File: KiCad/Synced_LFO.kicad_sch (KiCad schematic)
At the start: 41 parts, among them J1 UP_Out, J2 CLK In, J3 BP_Inv_Out, J4 BP_Out, P1 B100K, P2 B100K, P3 B100K, P4 B100K, U1 TL072, U2 TL072

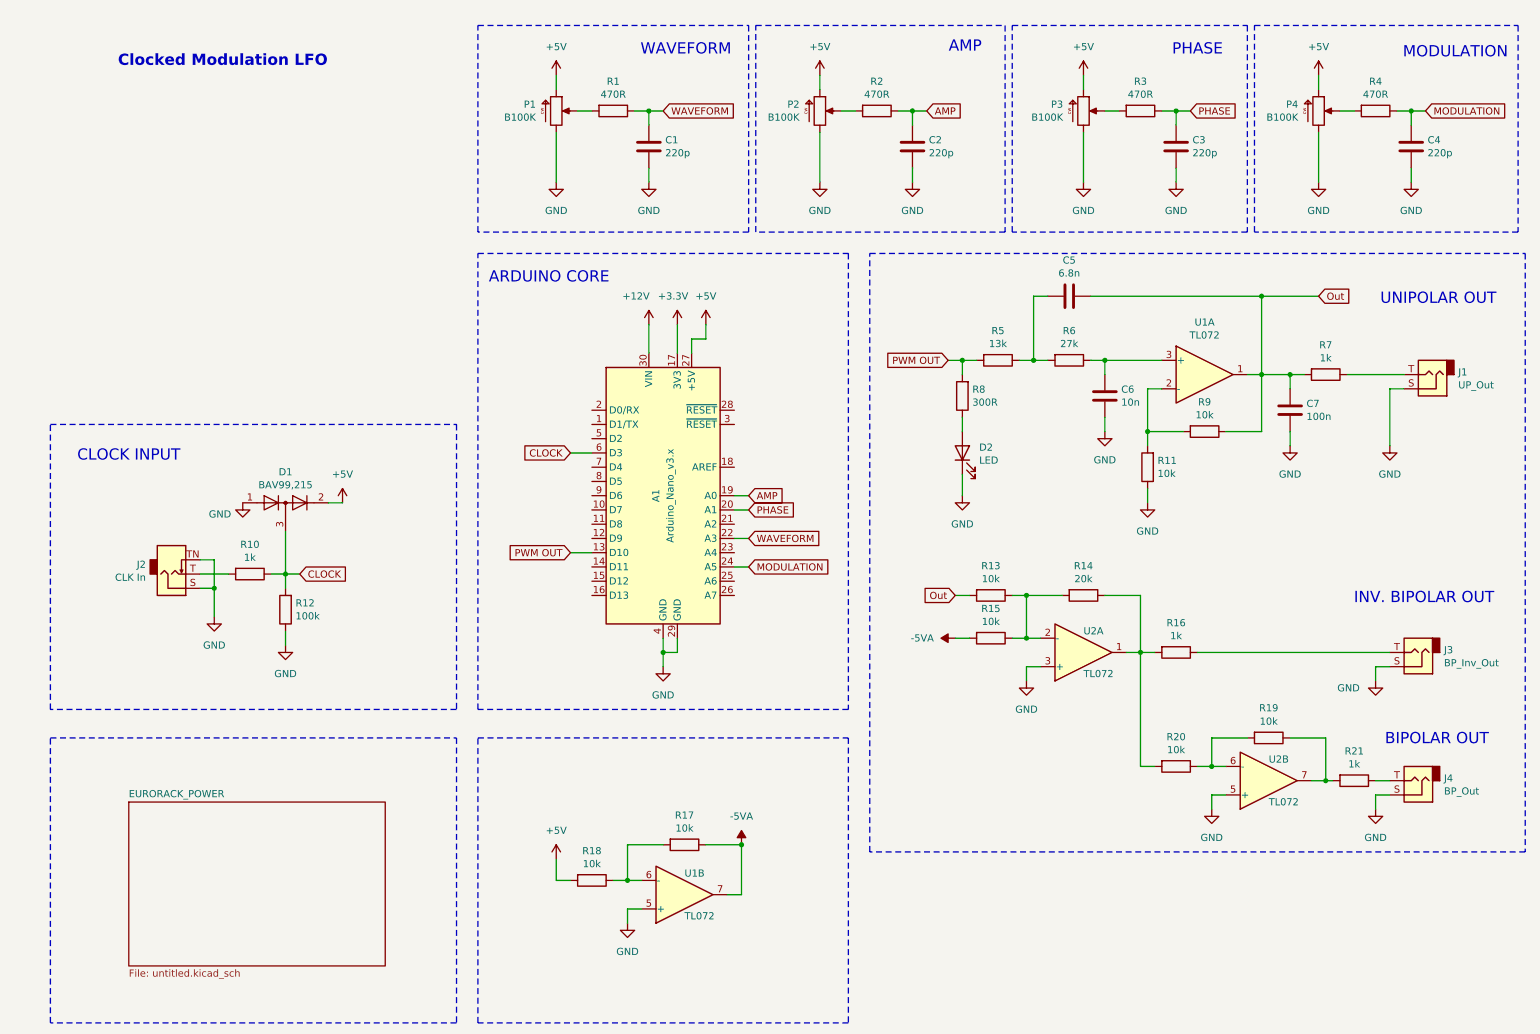
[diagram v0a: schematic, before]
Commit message: Added new Powerrail and fixed ERC Error
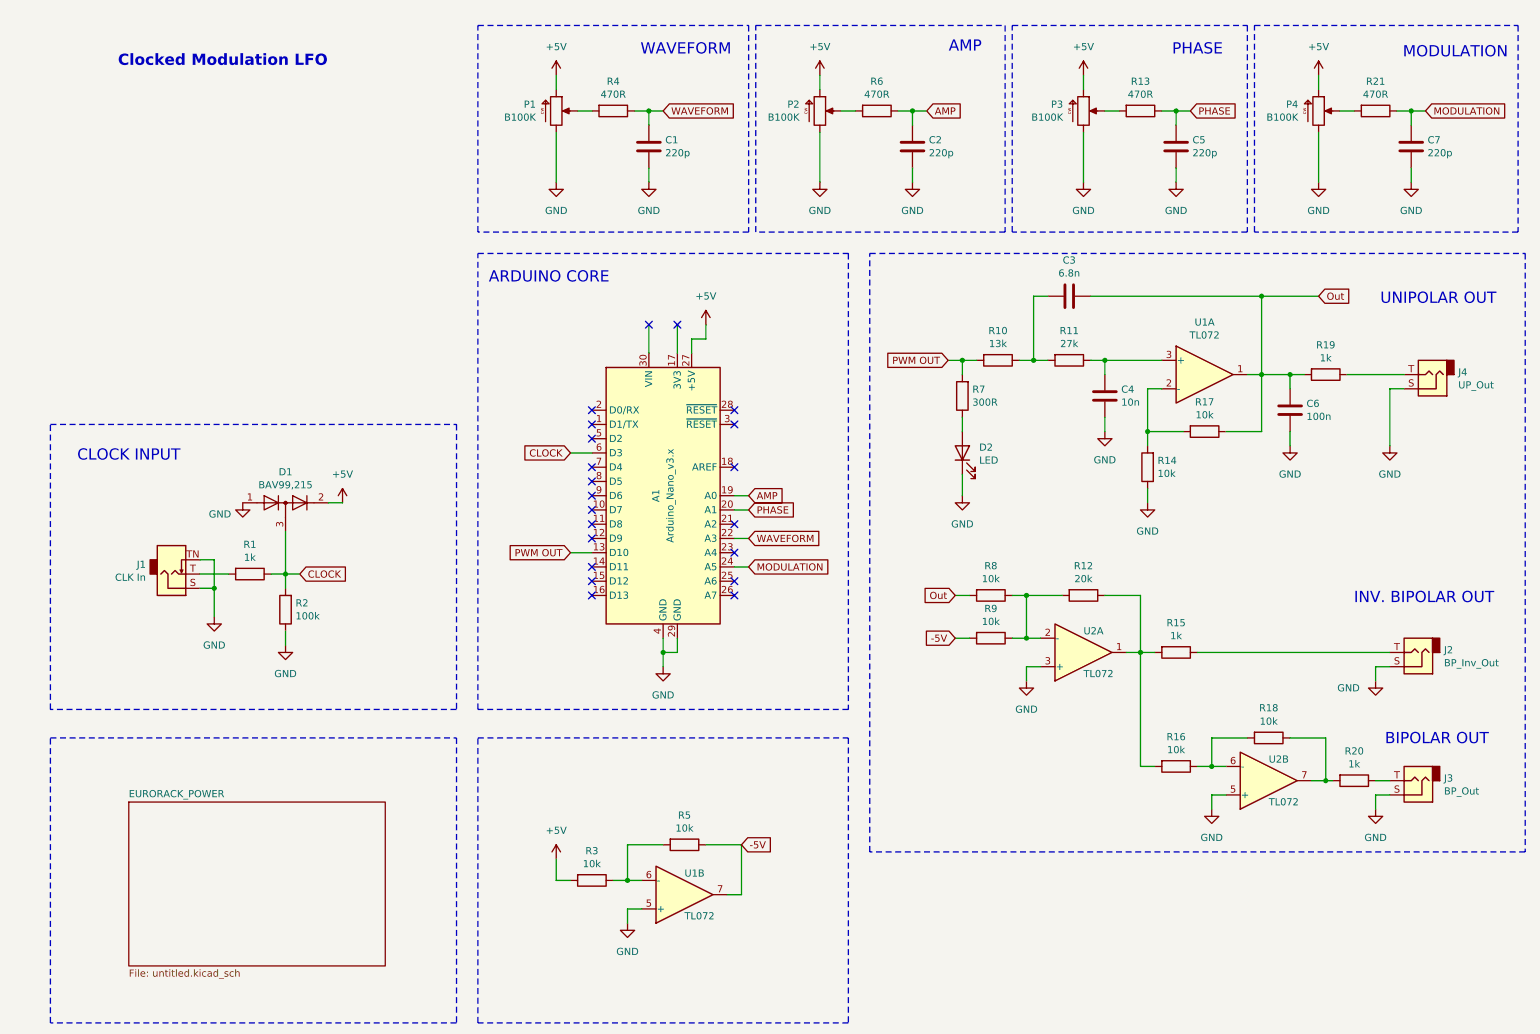
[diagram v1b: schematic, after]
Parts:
- renumbered C5 to C3, C6 to C4, C3 to C5, C7 to C6, C4 to C7, J2 to J1, J3 to J2, J4 to J3, J1 to J4, R10 to R1, R5 to R10, R6 to R11, R14 to R12, R3 to R13, R11 to R14, R16 to R15, R20 to R16, R9 to R17, R19 to R18, R7 to R19, R12 to R2, R21 to R20, R4 to R21, R18 to R3, R1 to R4, R17 to R5, R2 to R6, R8 to R7, R13 to R8, R15 to R9
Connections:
- net +12V: no longer names the net of A1.30 (VIN)
- net +3.3V: no longer names the net of A1.17 (3V3)
- net -5VA renamed -5V
- no-connect marks 0 -> 21

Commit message: adding footprints
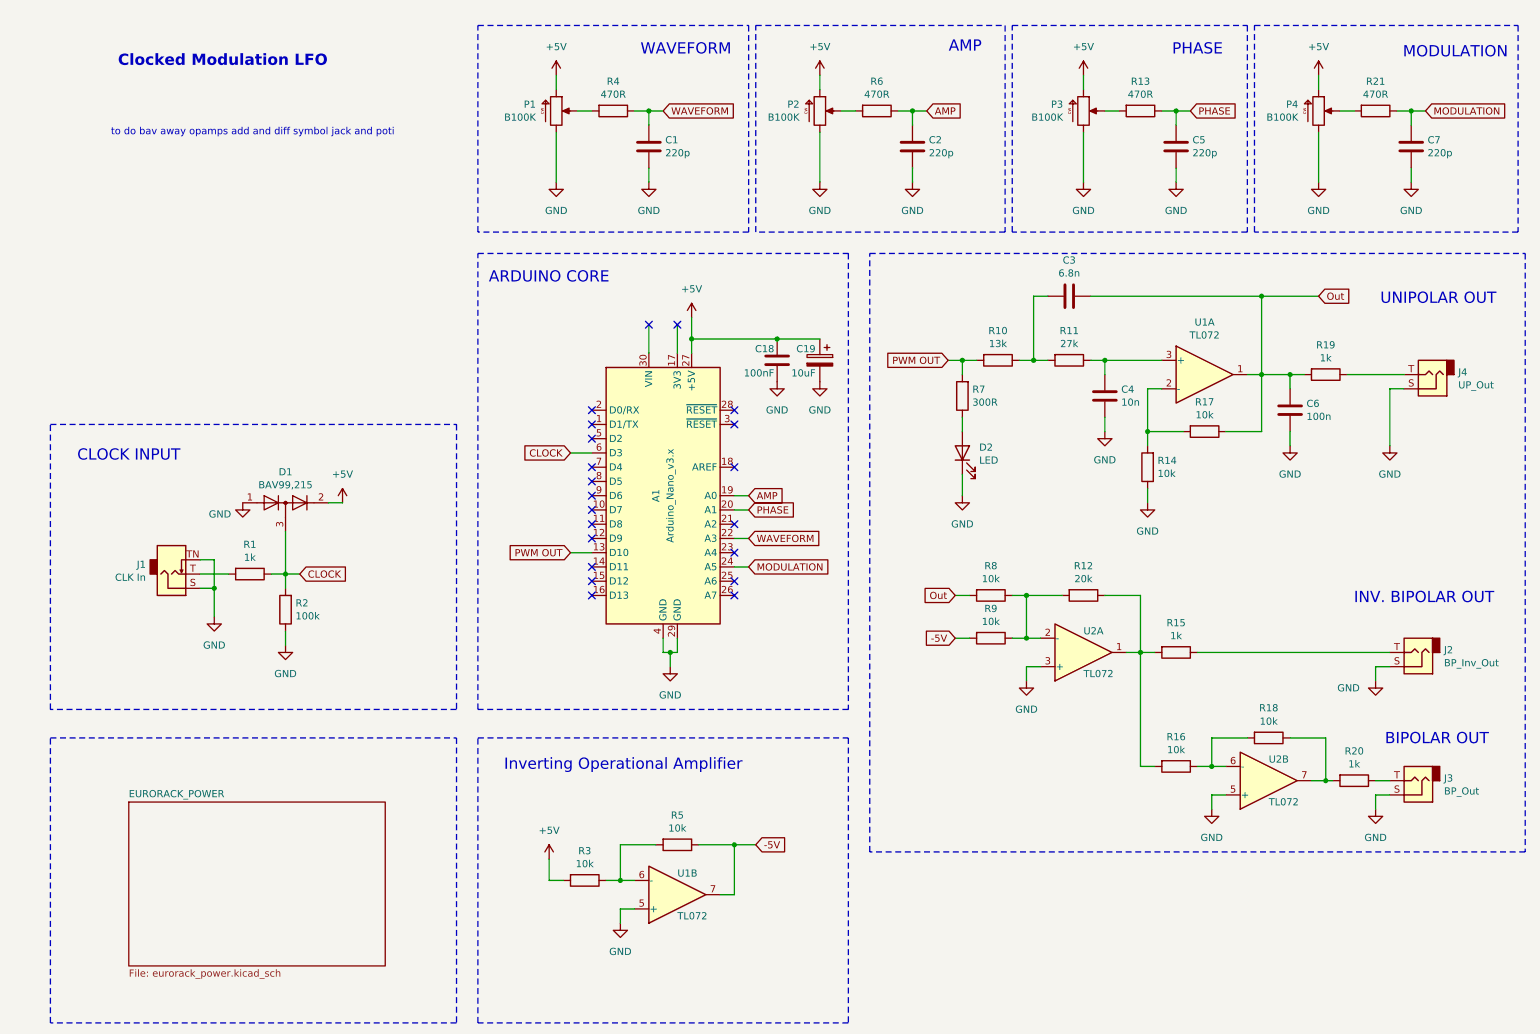
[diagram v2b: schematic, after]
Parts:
- added C18: 100nF, Capacitor_SMD:C_0805_2012Metric_Pad1.18x1.45mm_HandSolder, symbol Device:C
- added C19: 10uF, Capacitor_SMD:CP_Elec_5x5.4, symbol Device:C_Polarized
- A1: footprint Module:Arduino_Nano -> Eurorack:Arduino_Nano; now left out of the parts list
- C1, C2, C3, C4, C5, C6, C7: footprint Capacitor_SMD:C_0402_1005Metric -> Capacitor_SMD:C_0805_2012Metric_Pad1.18x1.45mm_HandSolder; now left out of the parts list
- D2: footprint LED_THT:LED_D3.0mm -> LED_THT:LED_D3.0mm_Clear; now left out of the parts list
- J1, J2, J3, J4: footprint Connector_Audio_QingPu:Jack_3.5mm_QingPu_WQP-PJ301M-12 -> Eurorack:Jack_3.5mm_QingPu_WQP-PJ398SM_Vertical; now left out of the parts list
- P1, P3, P4: footprint Potentiometer_THT_Additional:Potentiometer_AlpsAlpine_RK09L1140_wo_Fix -> Eurorack:Potentiometer_Alpha_RD901F_Vertical_Alt; now left out of the parts list
- P2: footprint Potentiometer_THT_Additional:Potentiometer_AlpsAlpine_RK09L1140 -> Eurorack:Potentiometer_Alpha_RD901F_Vertical_Alt; now left out of the parts list
- R1, R11, R12, R13, R14, R15, R16, R17, R18, R19, R2, R20, R21, R3, R4, R5, R6, R7, R8, R9: footprint Resistor_SMD:R_0402_1005Metric -> Resistor_SMD:R_0805_2012Metric_Pad1.20x1.40mm_HandSolder; now left out of the parts list
- R10: footprint Resistor_SMD:R_0603_1608Metric -> Resistor_SMD:R_0805_2012Metric_Pad1.20x1.40mm_HandSolder; now left out of the parts list
- U1, U2: now left out of the parts list
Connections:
- net +5V: now also C18.1, C19.1
- net GND: now also C18.2, C19.2
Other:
- sheet EURORACK_POWER: file untitled.kicad_sch -> eurorack_power.kicad_sch
- note added: "Inverting Operational Amplifier"
- note added: "to do bav away opamps add and diff symbol jack and poti"
- moved on the sheet: R3, R5, U1B

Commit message: adding last missing footprints
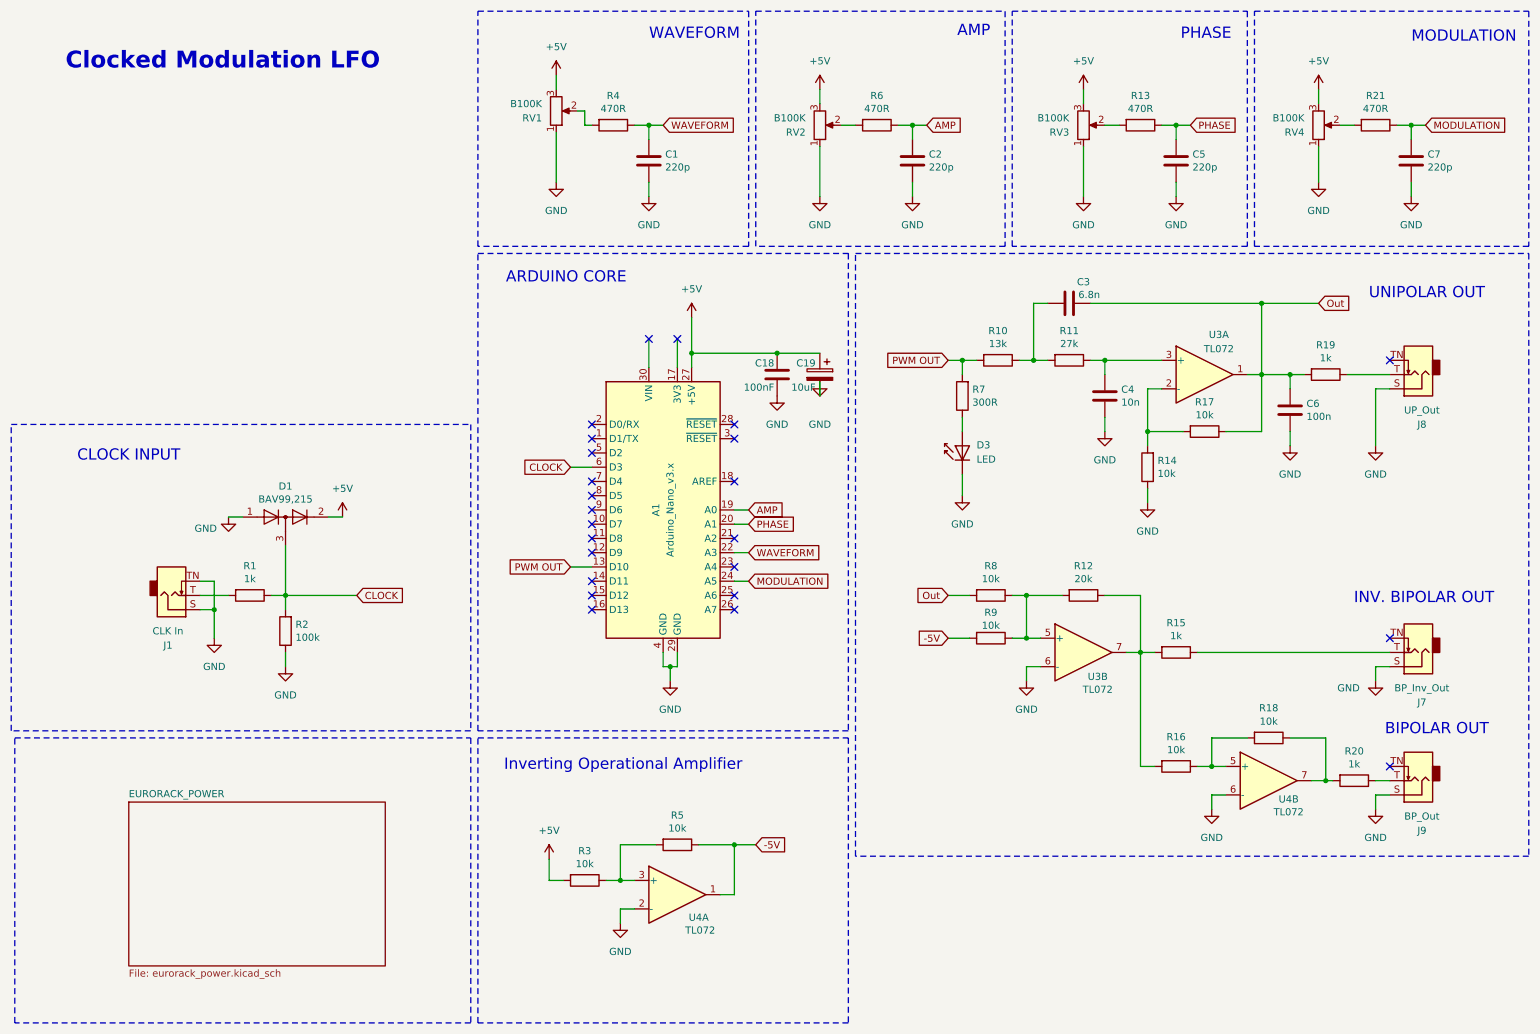
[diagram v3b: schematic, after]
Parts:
- removed D2: LED, LED_THT:LED_D3.0mm_Clear, symbol Device:LED
- removed J1: CLK In, Eurorack:Jack_3.5mm_QingPu_WQP-PJ398SM_Vertical, symbol Connector:AudioJack2_SwitchT
- removed J2: BP_Inv_Out, Eurorack:Jack_3.5mm_QingPu_WQP-PJ398SM_Vertical, symbol Connector:AudioJack2
- removed J3: BP_Out, Eurorack:Jack_3.5mm_QingPu_WQP-PJ398SM_Vertical, symbol Connector:AudioJack2
- removed J4: UP_Out, Eurorack:Jack_3.5mm_QingPu_WQP-PJ398SM_Vertical, symbol Connector:AudioJack2
- removed P1, P2, P3, P4: B100K, Eurorack:Potentiometer_Alpha_RD901F_Vertical_Alt, symbol Device_Additional:R_POT
- removed U1, U2: TL072, Package_SO:SOIC-8_3.9x4.9mm_P1.27mm, symbol Amplifier_Operational:TL072
- added D3: LED, LED_THT:LED_D3.0mm_Clear, symbol LED:IR204A
- added J1: CLK In, Eurorack:Jack_3.5mm_QingPu_WQP-PJ398SM_Vertical, symbol Connector_Audio:AudioJack2_SwitchT
- added J7: BP_Inv_Out, Eurorack:Jack_3.5mm_QingPu_WQP-PJ398SM_Vertical, symbol Connector_Audio:AudioJack2_SwitchT
- added J8: UP_Out, Eurorack:Jack_3.5mm_QingPu_WQP-PJ398SM_Vertical, symbol Connector_Audio:AudioJack2_SwitchT
- added J9: BP_Out, Eurorack:Jack_3.5mm_QingPu_WQP-PJ398SM_Vertical, symbol Connector_Audio:AudioJack2_SwitchT
- added RV1, RV2, RV3, RV4: B100K, Eurorack:Potentiometer_Alpha_RD901F_Vertical_Alt, symbol Device:R_Potentiometer
- added U3, U4: TL072, Package_SO:SOIC-8_3.9x4.9mm_P1.27mm, symbol Amplifier_Operational:TL072
- D1: now left out of the parts list
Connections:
- net +5V: now also RV1.3, RV2.3, RV3.3, RV4.3
- net -5V: now also U4.1
- net GND: now also D3.1 (K), J1.S, J1.TN, J7.S, J8.S, J9.S, RV1.1, RV2.1, RV3.1, RV4.1, U3.6 (-), U4.2 (-), U4.6 (-)
- net Out: now also U3.1
- net at R4.2: now also RV1.2
- net at R6.2: now also RV2.2
- net at R13.2: now also RV3.2
- net at R21.2: now also RV4.2
- net at R1.2: now also J1.T
- net at C4.2, R11.1: now also U3.3 (+)
- net at R14.2, R17.2: now also U3.2 (-)
- net at R19.1: now also J8.T
- net at R3.1, R5.2: now also U4.3 (+)
- net at R12.1, R15.2, R16.2: now also U3.7
- net at R12.2, R8.1, R9.1: now also U3.5 (+)
- net at R15.1: now also J7.T
- net at R16.1, R18.2: now also U4.5 (+)
- net at R18.1, R20.2: now also U4.7
- net at R20.1: now also J9.T
- net at R7.1: now also D3.2 (A)
- no-connect marks 21 -> 24
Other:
- note removed: "to do bav away opamps add and diff symbol jack and poti"
- moved on the sheet: A1, C1, C18, C19, C2, C3, C5, C7, D1, R1, R13, R2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

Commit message: adding new logo
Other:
- company: (none) -> © Dirty Dream – Nathanael Noir
- title: Clocked Modulation LFO -> Chronophase LFO
